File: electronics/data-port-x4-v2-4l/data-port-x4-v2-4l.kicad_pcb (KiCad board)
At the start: 4 copper layers, 100 x 70 mm, 219 parts, among them J1 LEAD, J101 PORT1, J102 PINS1, J201 PORT2, J202 PINS2, J301 PORT3, J302 PINS3, J401 PORT4, J402 PINS4, Q1 2N7002, Q2 2N7002, Q3 2N7002, U1 USB2517I-JZX, U10 TCA9534APWR, U101 TPS2553DBVR-1, U102 INA226AIDGSR, U103 USBLC6-2SC6, U105 H5VU25UC, U106 H5VU25UC, U107 LSF0108RKSR, U11 RP2354B, U2 TCA6408ARGTR, U201 TPS2553DBVR-1, U202 INA226AIDGSR, U203 USBLC6-2SC6, U205 H5VU25UC, U206 H5VU25UC, U207 LSF0108RKSR, U3 AP2114H-3.3TRG1, U301 TPS2553DBVR-1, U302 INA226AIDGSR, U303 USBLC6-2SC6, U305 H5VU25UC, U306 H5VU25UC, U307 LSF0108RKSR, U4 H5VU25UC, U401 TPS2553DBVR-1, U402 INA226AIDGSR, U403 USBLC6-2SC6, U405 H5VU25UC, U406 H5VU25UC, U407 LSF0108RKSR, U6 TCA6408ARGTR, U7 CH446Q, U8 CH446Q, U9 TPS60400DBVR, Y1 X322524MSB4SI, Y2 ABM8-272-T3

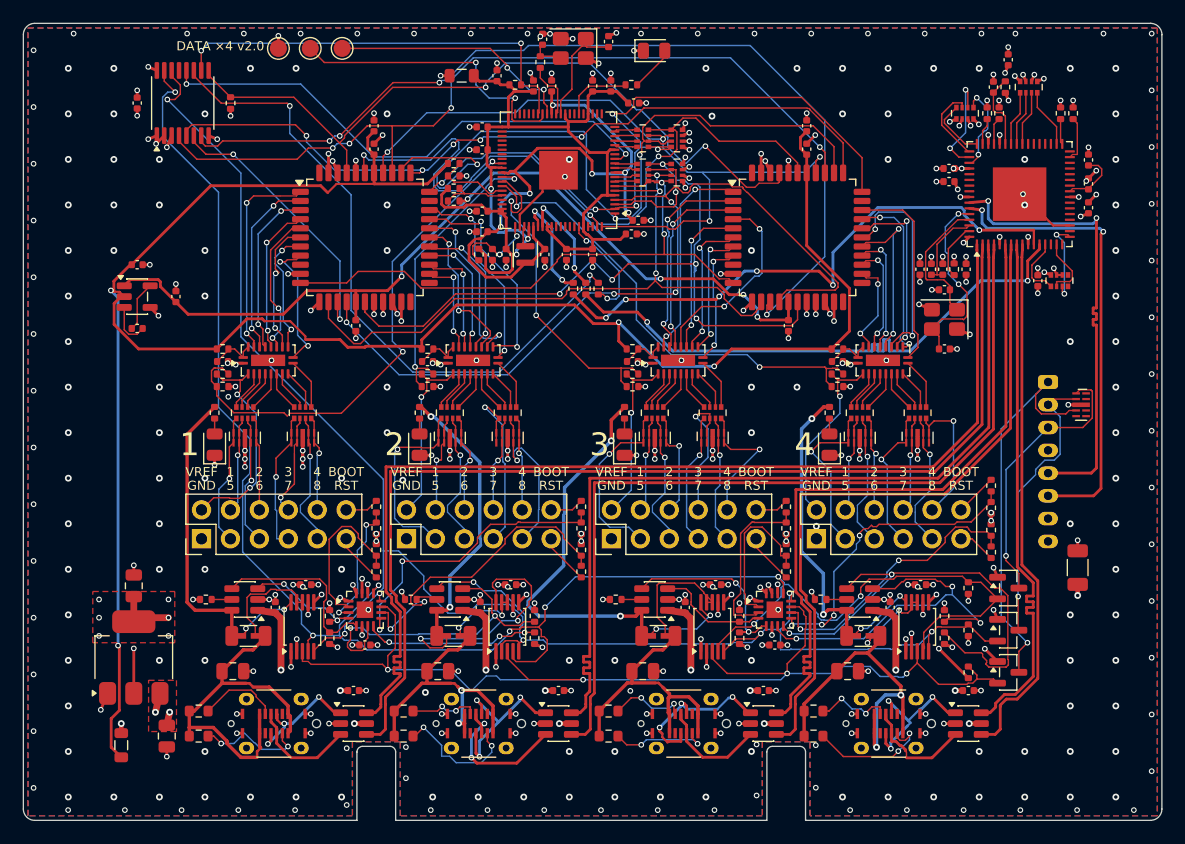
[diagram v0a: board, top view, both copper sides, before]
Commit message: DATA x4 v2 4-layer build: re-routed with no via in a small part's pad
The kept 4-layer build (electronics/data-port-x4-v2-4l) had 18 vias in
0402/0603 pads and one in a 0.4 mm pin.  JLC fills vias for free only from
6 layers.  With the pipeline's fix (previous commit), the same 16-setting
portfolio, optimizer off, gives 4 clean runs; ripup30-order2 is installed.

- 749 vias, 5194 mm, 1932 bends; 0 open, copper DRC 0, parity 0, ERC 0.
- Vias in pads: only the 8 drawn in the QFNs' thermal pads, accepted
  unfilled.
- The High-Speed pairs are unchanged (drawn, on F.Cu over GND).
- Gerbers and renders regenerated; BOM and CPL unchanged.
- Docs: the runs, where the vias in pads came from and the fix, and the
  +3V3_CP island as a fanned-out plane, tried and dropped.

The 6-layer board, the rack's, is untouched.

Co-Authored-By: Claude Opus 5.5 <noreply@anthropic.com>
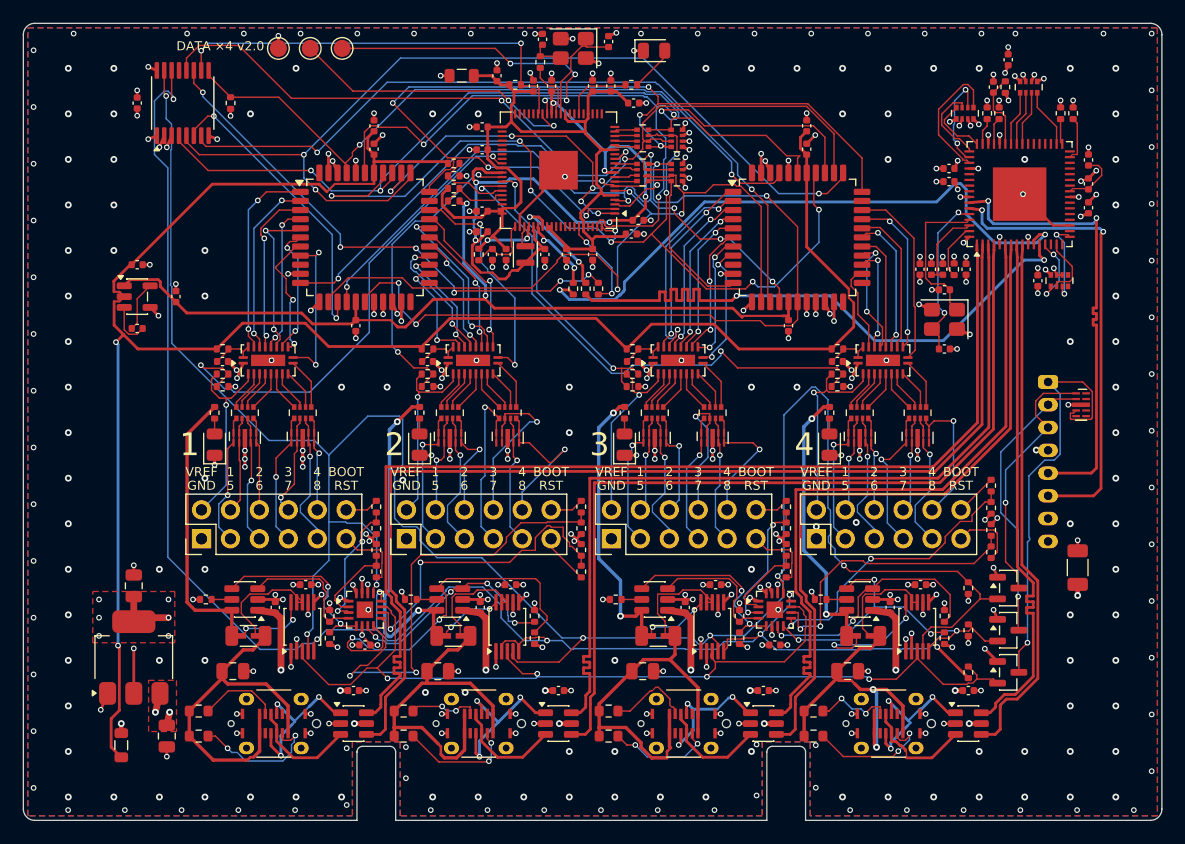
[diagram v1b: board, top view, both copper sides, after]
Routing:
- net SDA: track 160.7 -> 199.1 mm, vias 8 -> 7
- net BUS_D: track 64.1 -> 83.9 mm, vias 5 -> 6
- net PORT4_FLT_N: track 41.1 -> 22.1 mm, vias 2 -> 3
- net BUS_B: track 63.7 -> 81.6 mm, vias 4 -> 9
- net BUS_F: track 79.3 -> 62.0 mm, vias 4 -> 6
- net /Port 2/PORT2_SNS_P: track 21.8 -> 5.79 mm
- net /Matrix/MX_STB2: track 82.2 -> 66.9 mm, vias 4 -> 2
- net /Matrix/MX_CK: track 67.7 -> 81.6 mm, vias 5 -> 3
- net PORT2_BOOT_IO: track 26.2 -> 40.1 mm
- net SCL: track 141.7 -> 155.0 mm
- net CP_BOOT_N: track 58.3 -> 46.4 mm, vias 2 -> 6
- net PORT4_EN: track 32.8 -> 22.0 mm, vias 3 -> 2
- net /Port 3/PORT3_5V_SW: track 33.8 -> 24.7 mm
- net +5V_MX: track 182.2 -> 173.9 mm, vias 4 -> 2
- net PORT2_FLT_N: track 26.2 -> 33.9 mm, vias 4 -> 2
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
